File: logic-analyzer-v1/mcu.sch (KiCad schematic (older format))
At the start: 19 parts

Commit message: adding mod spi
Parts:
- added D?: LED, symbol Device:LED
- added J?: Conn_01x04_Male, symbol Connector:Conn_01x02_Male
- added R?: 100R, Resistor_SMD:R_0603_1608Metric_Pad1.05x0.95mm_HandSolder, symbol Device:R
- added R?: 1k, Resistor_SMD:R_0603_1608Metric_Pad1.05x0.95mm_HandSolder, symbol Device:R
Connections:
- net +3V3: now also R?.1
- net GND: now also D?.1 (K)
- net SPI_CS_0: now reaches U?.10 (PA0)
- net SPI_CS_1: now reaches U?.11 (PA1)
- net debug_led: now reaches U?.2 (PC13)
- net debug_led: now also R?.2
- net BOOT0: now reaches R?.2, U?.44 (BOOT0)
- net BOOT0: now also J?.2 (Pin_2)
- new net: J?.1 (Pin_1), R?.2
- new net: D?.2 (A), R?.1
- no-connect marks 14 -> 11
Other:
- moved on the sheet: J?
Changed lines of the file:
@@
 L Connector:Conn_01x04_Male J?
 U 1 1 5F1AF296
-P 10700 2700
-F 0 "J?" H 10800 3050 50  0000 C CNN
-F 1 "Conn_01x04_Male" H 10800 2950 50  0000 C CNN
-F 2 "" H 10700 2700 50  0001 C CNN
-F 3 "~" H 10700 2700 50  0001 C CNN
-	1    10700 2700
+P 10700 2900
+F 0 "J?" H 10800 3250 50  0000 C CNN
+F 1 "Conn_01x04_Male" H 10800 3150 50  0000 C CNN
+F 2 "" H 10700 2900 50  0001 C CNN
+F 3 "~" H 10700 2900 50  0001 C CNN
+	1    10700 2900
 	-1   0    0    -1
 $EndComp
-Connection ~ 5600 2300
 $Comp
 L Device:C C?
@@
 	1200 1350 1200 1500
 Wire Wire Line
-	5700 5300 5600 5300
-Connection ~ 5600 5300
-Wire Wire Line
 	2150 1900 2150 1800
 Wire Wire Line
@@
 Wire Wire Line
 	1600 1350 1800 1350
-Connection ~ 5700 2300
-Connection ~ 5500 2300
-Wire Wire Line
-	5400 2300 5500 2300
-Wire Wire Line
-	5500 2300 5600 2300
-Connection ~ 5500 5300
-Wire Wire Line
-	5500 5300 5600 5300
-Wire Wire Line
-	5400 5300 5500 5300
-Wire Wire Line
-	5800 2300 5700 2300
-Wire Wire Line
-	5600 2300 5700 2300
-$Comp
-L MCU_ST_STM32F1:STM32F102C8Tx U?
-U 1 1 5F196629
-P 5600 3800
-F 0 "U?" H 5500 4450 50  0000 C CNN
-F 1 "STM32F102C8Tx" H 5750 4300 50  0000 C CNN
-F 2 "Package_QFP:LQFP-48_7x7mm_P0.5mm" H 5000 2400 50  0001 R CNN
-F 3 "https://www.st.com/resource/en/datasheet/stm32f102c8.pdf" H 5600 3800 50  0001 C CNN
-F 4 "https://www.st.com/resource/en/application_note/cd00221665-oscillator-design-guide-for-stm8af-al-s-stm32-mcus-and-mpus-stmicroelectronics.pdf" H 5600 3800 50  0001 C CNN "Oscillator design"
-F 5 "https://www.st.com/resource/en/application_note/cd00164185-getting-started-with-stm32f10xxx-hardware-development-stmicroelectronics.pdf" H 5600 3800 50  0001 C CNN "Application note"
-	1    5600 3800
-	1    0    0    -1
-$EndComp
 Text Label 4800 2900 2    50   ~ 0
 OSC_IN
@@
 Wire Wire Line
 	2900 4150 2900 4200
-Text Notes 10250 3050 0    50   ~ 0
-debug connector
-Text Label 10100 2700 0    50   ~ 0
+Text Label 10100 2900 0    50   ~ 0
 GND
-Text Label 10100 2600 0    50   ~ 0
+Text Label 10100 2800 0    50   ~ 0
 SWCLK
-Text Label 10100 2800 0    50   ~ 0
+Text Label 10100 3000 0    50   ~ 0
 SWDIO
-Text Label 10100 2900 0    50   ~ 0
+Text Label 10100 3100 0    50   ~ 0
 NRST
 Wire Wire Line
@@
 $EndComp
 Wire Wire Line
-	10500 2600 10100 2600
-Wire Wire Line
-	10500 2700 10100 2700
-Wire Wire Line
 	10500 2800 10100 2800
 Wire Wire Line
 	10500 2900 10100 2900
+Wire Wire Line
+	10500 3000 10100 3000
+Wire Wire Line
+	10500 3100 10100 3100
 Wire Wire Line
 	3100 4150 2900 4150
 Connection ~ 2900 4150
-Connection ~ 5400 2300
 Connection ~ 1200 1350
 Wire Wire Line
@@
 Wire Wire Line
 	3100 4700 4900 4700
-$Comp
-L Device:R R?
-U 1 1 5F415484
-P 4500 2700
-AR Path="/5F08ED8D/5F415484" Ref="R?"  Part="1"
-AR Path="/5F19654C/5F415484" Ref="R?"  Part="1"
-F 0 "R?" V 4400 2800 50  0000 C CNN
-F 1 "4k7" V 4400 2600 50  0000 C CNN
-F 2 "Resistor_SMD:R_0603_1608Metric_Pad1.05x0.95mm_HandSolder" V 4430 2700 50  0001 C CNN
-F 3 "~" H 4500 2700 50  0001 C CNN
-	1    4500 2700
-	0    -1   1    0
-$EndComp
 Wire Wire Line
 	4200 2900 4200 2700
-Wire Wire Line
-	4200 2700 4350 2700
-Wire Wire Line
-	4650 2700 4900 2700
 Connection ~ 2250 1450
 Wire Wire Line
@@
 Wire Wire Line
 	5400 5400 5400 5300
-Connection ~ 5400 5300
 Wire Wire Line
 	6750 4700 6200 4700
@@
 Wire Wire Line
 	4500 3600 4900 3600
-NoConn ~ 4900 3200
 NoConn ~ 4900 3300
 NoConn ~ 4900 3400
@@
 NoConn ~ 4900 5000
 NoConn ~ 4900 5100
-NoConn ~ 6200 3600
-NoConn ~ 6200 3700
 NoConn ~ 6200 4000
 NoConn ~ 6200 4400
@@
 L Connector:Conn_01x03_Male J?
 U 1 1 5F5072CB
-P 10700 3500
-F 0 "J?" H 10800 3850 50  0000 C CNN
-F 1 "Conn_01x04_Male" H 10800 3750 50  0000 C CNN
-F 2 "" H 10700 3500 50  0001 C CNN
-F 3 "~" H 10700 3500 50  0001 C CNN
-	1    10700 3500
+P 10700 3700
+F 0 "J?" H 10800 4050 50  0000 C CNN
+F 1 "Conn_01x04_Male" H 10800 3950 50  0000 C CNN
+F 2 "" H 10700 3700 50  0001 C CNN
+F 3 "~" H 10700 3700 50  0001 C CNN
+	1    10700 3700
 	-1   0    0    -1
 $EndComp
 Wire Wire Line
-	10500 3400 10100 3400
-Wire Wire Line
-	10500 3500 10100 3500
-Wire Wire Line
 	10500 3600 10100 3600
+Wire Wire Line
+	10500 3700 10100 3700
+Wire Wire Line
+	10500 3800 10100 3800
 $Comp
 L power:GND #PWR?
 U 1 1 5F515523
-P 10100 3600
-F 0 "#PWR?" H 10100 3350 50  0001 C CNN
-F 1 "GND" H 10105 3427 50  0000 C CNN
-F 2 "" H 10100 3600 50  0001 C CNN
-F 3 "" H 10100 3600 50  0001 C CNN
-	1    10100 3600
-	1    0    0    -1
-$EndComp
-Text Label 10100 3400 0    50   ~ 0
+P 10100 3800
+F 0 "#PWR?" H 10100 3550 50  0001 C CNN
+F 1 "GND" H 10105 3627 50  0000 C CNN
+F 2 "" H 10100 3800 50  0001 C CNN
+F 3 "" H 10100 3800 50  0001 C CNN
+	1    10100 3800
+	1    0    0    -1
+$EndComp
+Text Label 10100 3600 0    50   ~ 0
 USART1_TX
-Text Label 10100 3500 0    50   ~ 0
+Text Label 10100 3700 0    50   ~ 0
 USART1_RX
+$Comp
+L Connector:Conn_01x02_Male J?
+U 1 1 5F41AB6E
+P 10700 4400
+F 0 "J?" H 10800 4750 50  0000 C CNN
+F 1 "Conn_01x04_Male" H 10800 4650 50  0000 C CNN
+F 2 "" H 10700 4400 50  0001 C CNN
+F 3 "~" H 10700 4400 50  0001 C CNN
+	1    10700 4400
+	-1   0    0    -1
+$EndComp
+Text Notes 10100 3250 0    50   ~ 0
+debug connector
+$Comp
+L Device:R R?
+U 1 1 5F41D440
+P 10200 4350
+AR Path="/5F08ED8D/5F41D440" Ref="R?"  Part="1"
+AR Path="/5F19654C/5F41D440" Ref="R?"  Part="1"
+F 0 "R?" V 10100 4450 50  0000 C CNN
+F 1 "100R" V 10100 4250 50  0000 C CNN
+F 2 "Resistor_SMD:R_0603_1608Metric_Pad1.05x0.95mm_HandSolder" V 10130 4350 50  0001 C CNN
+F 3 "~" H 10200 4350 50  0001 C CNN
+	1    10200 4350
+	0    -1   1    0
+$EndComp
+$Comp
+L power:+3V3 #PWR?
+U 1 1 5F41E950
+P 9850 4350
+F 0 "#PWR?" H 9850 4200 50  0001 C CNN
+F 1 "+3V3" H 9865 4523 50  0000 C CNN
+F 2 "" H 9850 4350 50  0001 C CNN
+F 3 "" H 9850 4350 50  0001 C CNN
+	1    9850 4350
+	1    0    0    -1
+$EndComp
+Wire Wire Line
+	4650 2700 4750 2700
+Wire Wire Line
+	4200 2700 4350 2700
+$Comp
+L Device:R R?
+U 1 1 5F415484
+P 4500 2700
+AR Path="/5F08ED8D/5F415484" Ref="R?"  Part="1"
+AR Path="/5F19654C/5F415484" Ref="R?"  Part="1"
+F 0 "R?" V 4400 2800 50  0000 C CNN
+F 1 "4k7" V 4400 2600 50  0000 C CNN
+F 2 "Resistor_SMD:R_0603_1608Metric_Pad1.05x0.95mm_HandSolder" V 4430 2700 50  0001 C CNN
+F 3 "~" H 4500 2700 50  0001 C CNN
+	1    4500 2700
+	0    -1   1    0
+$EndComp
+Wire Wire Line
+	4750 2700 4750 2250
+Wire Wire Line
+	4750 2250 3700 2250
+Connection ~ 4750 2700
+Wire Wire Line
+	4750 2700 4900 2700
+Text Label 3700 2250 0    50   ~ 0
+BOOT0
+Text Label 10100 4500 0    50   ~ 0
+BOOT0
+Wire Wire Line
+	10100 4500 10500 4500
+Wire Wire Line
+	9850 4350 10050 4350
+Wire Wire Line
+	10350 4350 10350 4400
+Wire Wire Line
+	10350 4400 10500 4400
+Wire Wire Line
+	5700 5300 5600 5300
+Connection ~ 5600 5300
+Wire Wire Line
+	5400 5300 5500 5300
+Wire Wire Line
+	5500 5300 5600 5300
+Connection ~ 5500 5300
+Connection ~ 5400 5300
+Wire Wire Line
+	5800 2300 5700 2300
+Connection ~ 5700 2300
+Wire Wire Line
+	5600 2300 5700 2300
+Connection ~ 5600 2300
+Wire Wire Line
+	5500 2300 5600 2300
+Wire Wire Line
+	5400 2300 5500 2300
+Connection ~ 5500 2300
+Connection ~ 5400 2300
+$Comp
+L MCU_ST_STM32F1:STM32F102C8Tx U?
+U 1 1 5F196629
+P 5600 3800
+F 0 "U?" H 5500 4450 50  0000 C CNN
+F 1 "STM32F102C8Tx" H 5750 4300 50  0000 C CNN
+F 2 "Package_QFP:LQFP-48_7x7mm_P0.5mm" H 5000 2400 50  0001 R CNN
+F 3 "https://www.st.com/resource/en/datasheet/stm32f102c8.pdf" H 5600 3800 50  0001 C CNN
+F 4 "https://www.st.com/resource/en/application_note/cd00221665-oscillator-design-guide-for-stm8af-al-s-stm32-mcus-and-mpus-stmicroelectronics.pdf" H 5600 3800 50  0001 C CNN "Oscillator design"
+F 5 "https://www.st.com/resource/en/application_note/cd00164185-getting-started-with-stm32f10xxx-hardware-development-stmicroelectronics.pdf" H 5600 3800 50  0001 C CNN "Application note"
+	1    5600 3800
+	1    0    0    -1
+$EndComp
+Wire Wire Line
+	4900 3200 3700 3200
+Text Label 4400 3200 0    50   ~ 0
+debug_led
+$Comp
+L Device:LED D?
+U 1 1 5F4446F1
+P 3150 3200
+F 0 "D?" H 3143 3417 50  0000 C CNN
+F 1 "LED" H 3143 3326 50  0000 C CNN
+F 2 "" H 3150 3200 50  0001 C CNN
+F 3 "~" H 3150 3200 50  0001 C CNN
+	1    3150 3200
+	1    0    0    -1
+$EndComp
+Wire Wire Line
+	3400 3200 3300 3200
+$Comp
+L power:GND #PWR?
+U 1 1 5F45EC84
+P 2900 3300
+F 0 "#PWR?" H 2900 3050 50  0001 C CNN
+F 1 "GND" H 2905 3127 50  0000 C CNN
+F 2 "" H 2900 3300 50  0001 C CNN
+F 3 "" H 2900 3300 50  0001 C CNN
+	1    2900 3300
+	1    0    0    -1
+$EndComp
+Wire Wire Line
+	2900 3300 2900 3200
+Wire Wire Line
+	2900 3200 3000 3200
+$Comp
+L Device:R R?
+U 1 1 5F4452A2
+P 3550 3200
+AR Path="/5F08ED8D/5F4452A2" Ref="R?"  Part="1"
+AR Path="/5F19654C/5F4452A2" Ref="R?"  Part="1"
+F 0 "R?" V 3650 3050 50  0000 C CNN
+F 1 "1k" V 3650 3250 50  0000 C CNN
+F 2 "Resistor_SMD:R_0603_1608Metric_Pad1.05x0.95mm_HandSolder" V 3480 3200 50  0001 C CNN
+F 3 "~" H 3550 3200 50  0001 C CNN
+	1    3550 3200
+	0    -1   -1   0
+$EndComp
+Wire Wire Line
+	6200 3700 6750 3700
+Wire Wire Line
+	6200 3600 6750 3600
 Wire Bus Line
 	4400 3400 4400 4200
+Text Label 6300 3600 0    50   ~ 0
+SPI_CS_0
+Text Label 6300 3700 0    50   ~ 0
+SPI_CS_1
+Text HLabel 6750 3600 2    50   BiDi ~ 0
+SPI_CS_0
+Text HLabel 6750 3700 2    50   BiDi ~ 0
+SPI_CS_1
 $EndSCHEMATC

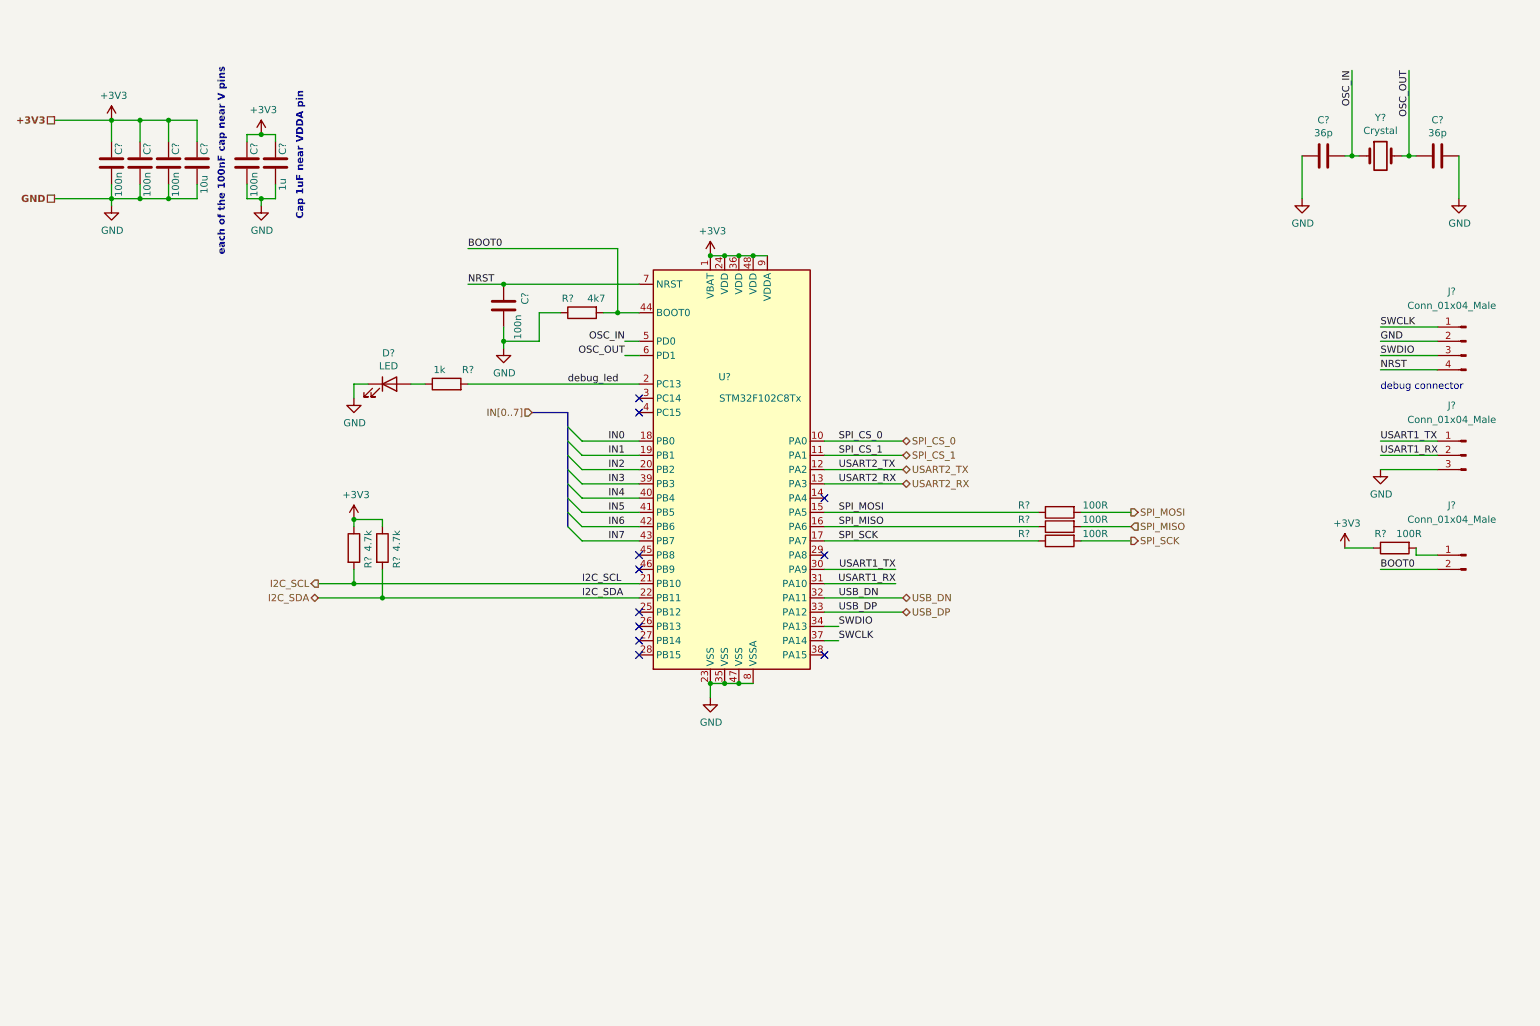
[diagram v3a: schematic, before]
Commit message: adding 2x spi memory
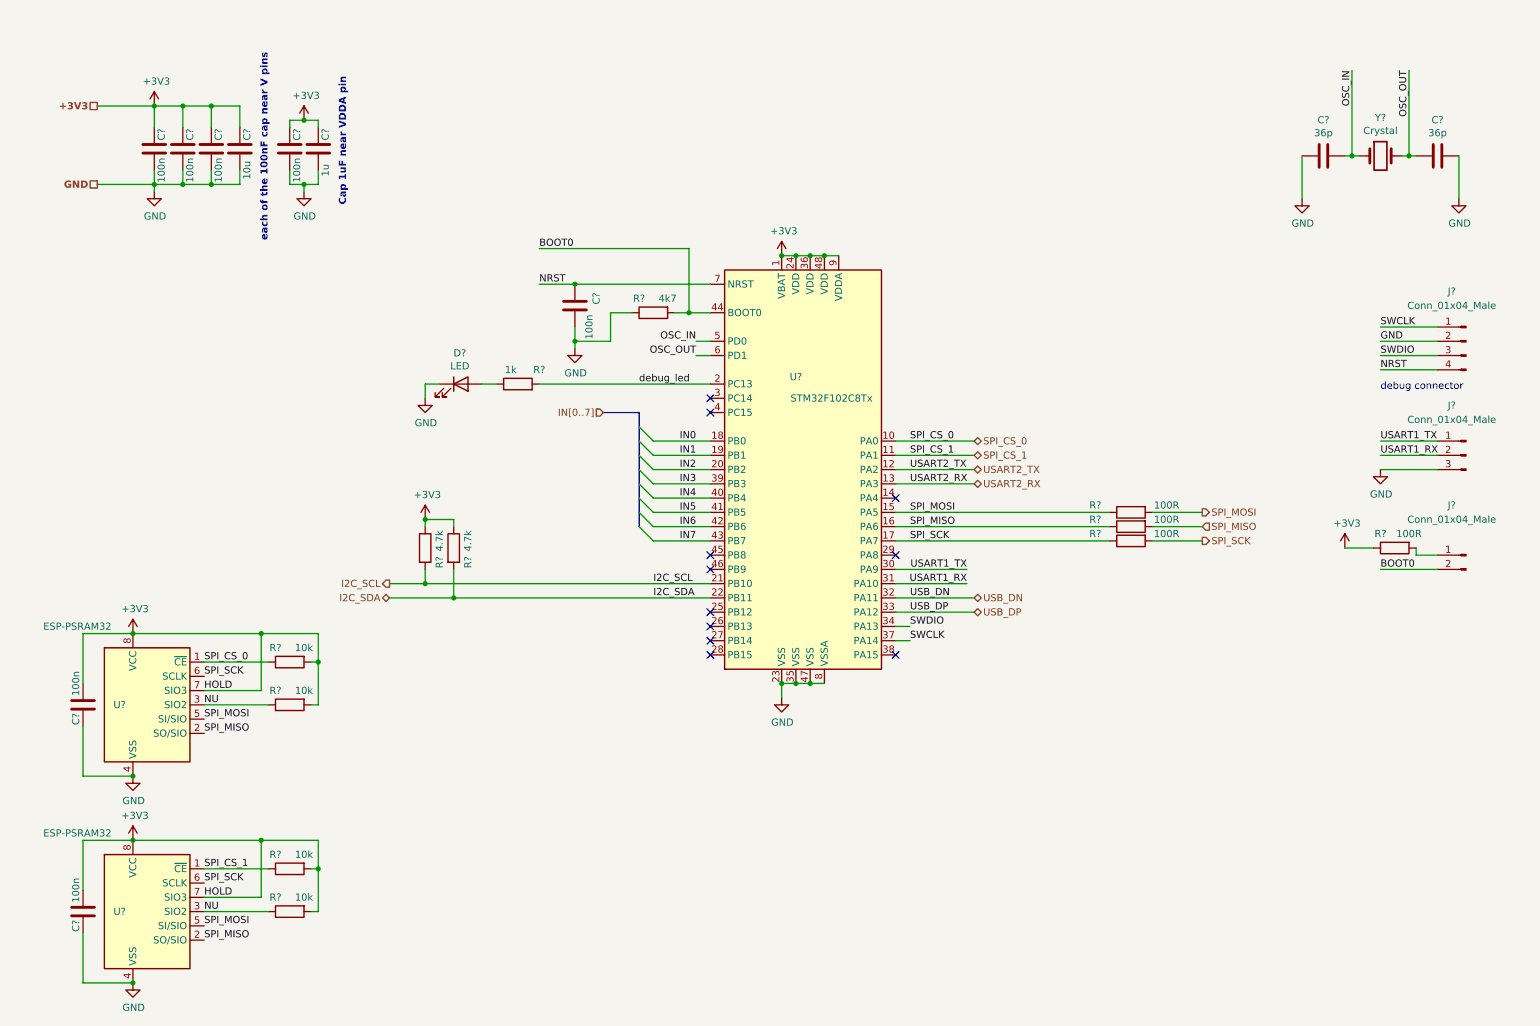
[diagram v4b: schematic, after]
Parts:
- added C? (x2): 100n, Capacitor_SMD:C_0603_1608Metric_Pad1.05x0.95mm_HandSolder, symbol Device:C
- added R? (x4): 10k, Resistor_SMD:R_0603_1608Metric_Pad1.05x0.95mm_HandSolder, symbol Device:R
- added U? (x2): ESP-PSRAM32, Package_SO:SOIC-8_3.9x4.9mm_P1.27mm, symbol Memory_RAM:ESP-PSRAM32
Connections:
- net +3V3: now also C?.1, C?.1, R?.2, R?.2, R?.2, R?.2, U?.7 (SIO3), U?.7 (SIO3), U?.8 (VCC), U?.8 (VCC)
- net GND: now also C?.2, C?.2, U?.4 (VSS), U?.4 (VSS)
- net SPI_CS_0: now also R?.1, U?.1 (~CE)
- net SPI_CS_1: now also R?.1, U?.1 (~CE)
- net SPI_MISO: now also U?.2 (SO/SIO), U?.2 (SO/SIO)
- net SPI_MOSI: now also U?.5 (SI/SIO), U?.5 (SI/SIO)
- net SPI_SCK: now also U?.6 (SCLK), U?.6 (SCLK)
- new net NU: R?.1, R?.1, U?.3 (SIO2), U?.3 (SIO2)
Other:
- moved on the sheet: C?, D?, R?, U?
